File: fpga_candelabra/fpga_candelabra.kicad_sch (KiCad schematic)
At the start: 0 parts

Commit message: Candelabra: Place all FPGA symbols
Signed-off-by: Yichuan Gao <gaoyichuan000@gmail.com>
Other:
- added sheet FPGA Bank 0 (fpga_bank_0.kicad_sch)
- added sheet FPGA Bank 61-64 (fpga_bank_61_64.kicad_sch)
- added sheet FPGA Bank 65-68 (fpga_bank_65_68.kicad_sch)
- added sheet FPGA Bank 69-72 (fpga_bank_69_72.kicad_sch)
- added sheet FPGA Bank 73-74 (fpga_bank_73_74.kicad_sch)
- added sheet FPGA Power (fpga_power.kicad_sch)
- added sheet FPGA Quad 124-133 (fpga_quad_124_133.kicad_sch)
- added sheet FPGA Quad 224-233 (fpga_quad_224_233.kicad_sch)
- added sheet Power VCCINT (power_vccint.kicad_sch)

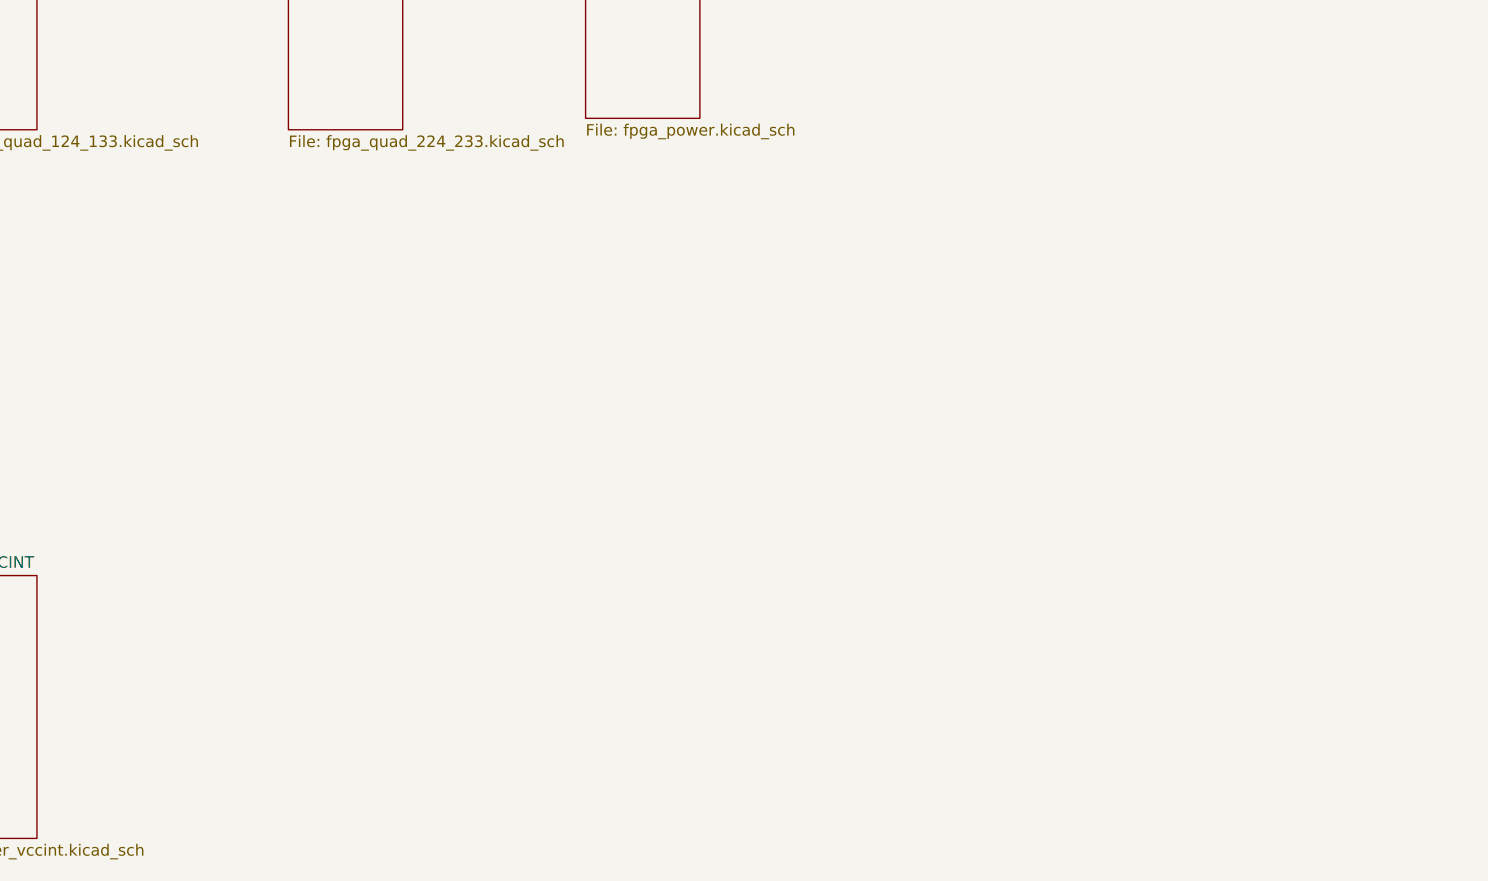
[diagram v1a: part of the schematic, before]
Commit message: fpga_candelabra: finish most FPGA & FMC VADJ power supplies
Signed-off-by: Yichuan Gao <gaoyichuan000@gmail.com>
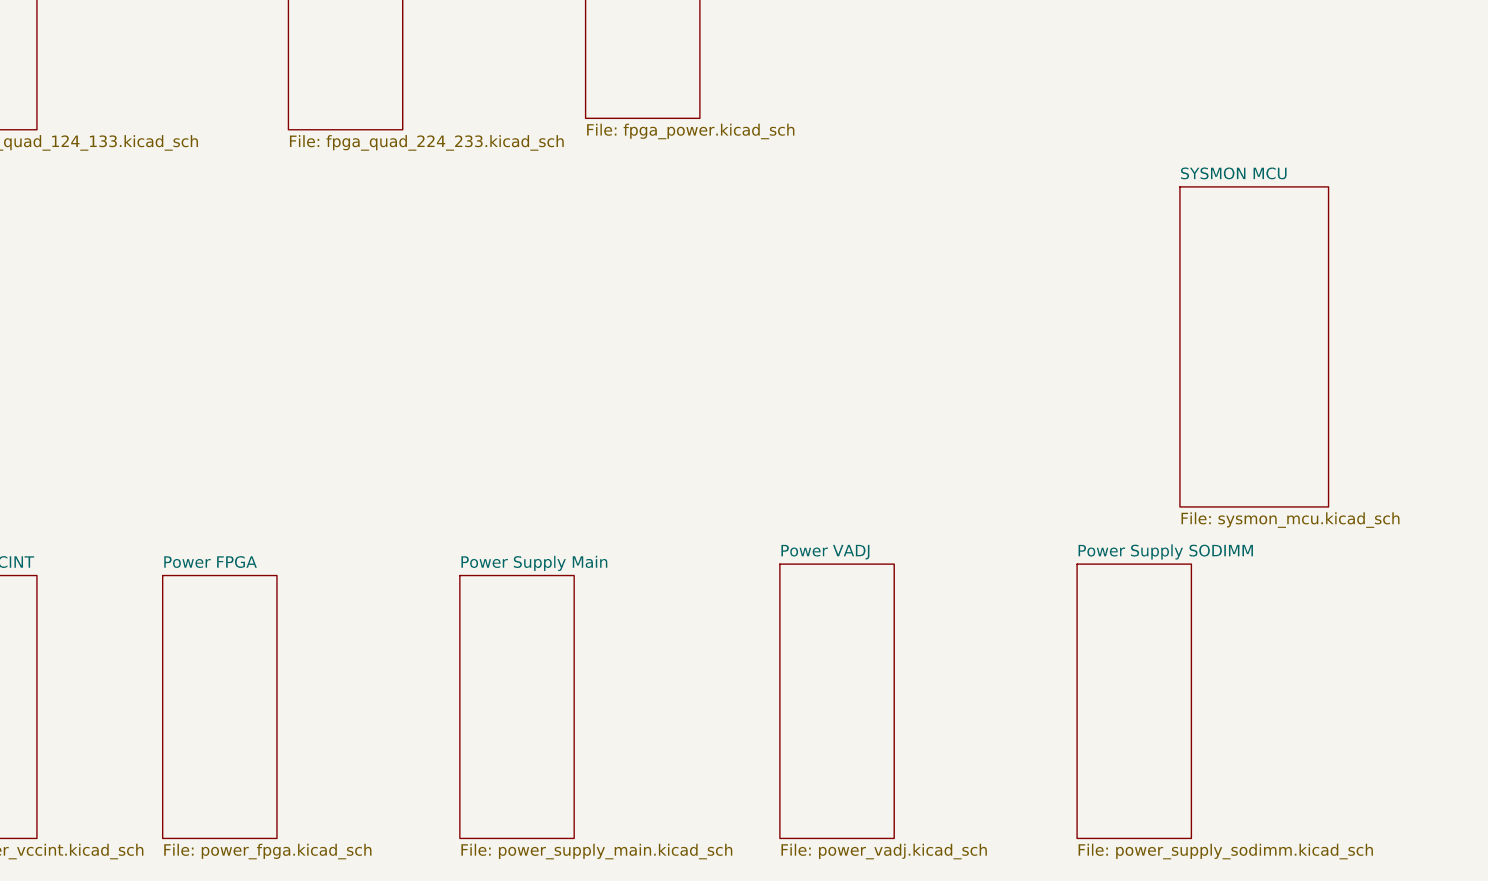
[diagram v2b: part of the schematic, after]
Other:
- added sheet Power FPGA (power_fpga.kicad_sch)
- added sheet Power Supply Main (power_supply_main.kicad_sch)
- added sheet Power Supply SODIMM (power_supply_sodimm.kicad_sch)
- added sheet Power VADJ (power_vadj.kicad_sch)
- added sheet SYSMON MCU (sysmon_mcu.kicad_sch)
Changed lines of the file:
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@@
+	)
+	(sheet
+		(at 151.13 134.62)
+		(size 12.7 30.48)
+		(fields_autoplaced yes)
+		(stroke
+			(width 0.1524)
+			(type solid)
+			(color 132 0 132 1)
+		)
+		(fill
+			(color 255 255 255 0.0000)
+		)
+		(property "Sheetname" "Power Supply SODIMM"
+			(at 151.13 133.9084 0)
+			(effects
+				(font
+					(size 1.27 1.27)
+				)
+				(justify left bottom)
+			)
+		)
+		(property "Sheetfile" "power_supply_sodimm.kicad_sch"
+			(at 151.13 165.6846 0)
+			(effects
+				(font
+					(size 1.27 1.27)
+				)
+				(justify left top)
+			)
+		)
+		(instances
+			(project "fpga_candelabra"
+				(path "/01ed9e92-4e50-4b41-90dc-10444aaec5f7"
+					(page "15")
+				)
+			)
+		)
 	)
 	(sheet
@@
 	)
 	(sheet
+		(at 82.55 135.89)
+		(size 12.7 29.21)
+		(fields_autoplaced yes)
+		(stroke
+			(width 0.1524)
+			(type solid)
+			(color 132 0 132 1)
+		)
+		(fill
+			(color 255 255 255 0.0000)
+		)
+		(property "Sheetname" "Power Supply Main"
+			(at 82.55 135.1784 0)
+			(effects
+				(font
+					(size 1.27 1.27)
+				)
+				(justify left bottom)
+			)
+		)
+		(property "Sheetfile" "power_supply_main.kicad_sch"
+			(at 82.55 165.6846 0)
+			(effects
+				(font
+					(size 1.27 1.27)
+				)
+				(justify left top)
+			)
+		)
+		(instances
+			(project "fpga_candelabra"
+				(path "/01ed9e92-4e50-4b41-90dc-10444aaec5f7"
+					(page "11")
+				)
+			)
+		)
+	)
+	(sheet
 		(at 22.86 59.69)
 		(size 12.7 26.67)
@@
 	)
 	(sheet
+		(at 162.56 92.71)
+		(size 16.51 35.56)
+		(fields_autoplaced yes)
+		(stroke
+			(width 0.1524)
+			(type solid)
+			(color 132 0 132 1)
+		)
+		(fill
+			(color 255 255 255 0.0000)
+		)
+		(property "Sheetname" "SYSMON MCU"
+			(at 162.56 91.9984 0)
+			(effects
+				(font
+					(size 1.27 1.27)
+				)
+				(justify left bottom)
+			)
+		)
+		(property "Sheetfile" "sysmon_mcu.kicad_sch"
+			(at 162.56 128.8546 0)
+			(effects
+				(font
+					(size 1.27 1.27)
+				)
+				(justify left top)
+			)
+		)
+		(instances
+			(project "fpga_candelabra"
+				(path "/01ed9e92-4e50-4b41-90dc-10444aaec5f7"
+					(page "10")
+				)
+			)
+		)
+	)
+	(sheet
 		(at 50.8 20.32)
 		(size 12.7 25.4)
@@
 	)
 	(sheet
+		(at 49.53 135.89)
+		(size 12.7 29.21)
+		(fields_autoplaced yes)
+		(stroke
+			(width 0.1524)
+			(type solid)
+			(color 132 0 132 1)
+		)
+		(fill
+			(color 255 255 255 0.0000)
+		)
+		(property "Sheetname" "Power FPGA"
+			(at 49.53 135.1784 0)
+			(effects
+				(font
+					(size 1.27 1.27)
+				)
+				(justify left bottom)
+			)
+		)
+		(property "Sheetfile" "power_fpga.kicad_sch"
+			(at 49.53 165.6846 0)
+			(effects
+				(font
+					(size 1.27 1.27)
+				)
+				(justify left top)
+			)
+		)
+		(instances
+			(project "fpga_candelabra"
+				(path "/01ed9e92-4e50-4b41-90dc-10444aaec5f7"
+					(page "13")
+				)
+			)
+		)
+	)
+	(sheet
 		(at 96.52 59.69)
 		(size 12.7 25.4)
@@
 			(project "fpga_candelabra"
 				(path "/01ed9e92-4e50-4b41-90dc-10444aaec5f7"
-					(page "10")
-				)
-			)
+					(page "12")
+				)
+			)
+		)
+	)
+	(sheet
+		(at 118.11 134.62)
+		(size 12.7 30.48)
+		(fields_autoplaced yes)
+		(stroke
+			(width 0.1524)
+			(type solid)
+			(color 132 0 132 1)
+		)
+		(fill
+			(color 255 255 255 0.0000)
+		)
+		(property "Sheetname" "Power VADJ"
+			(at 118.11 133.9084 0)
+			(effects
+				(font
+					(size 1.27 1.27)
+				)
+				(justify left bottom)
+			)
+		)
+		(property "Sheetfile" "power_vadj.kicad_sch"
+			(at 118.11 165.6846 0)
+			(effects
+				(font
+					(size 1.27 1.27)
+				)
+				(justify left top)
+			)
+		)
+		(instances
+			(project "fpga_candelabra"
+				(path "/01ed9e92-4e50-4b41-90dc-10444aaec5f7"
+					(page "14")
+				)
+			)

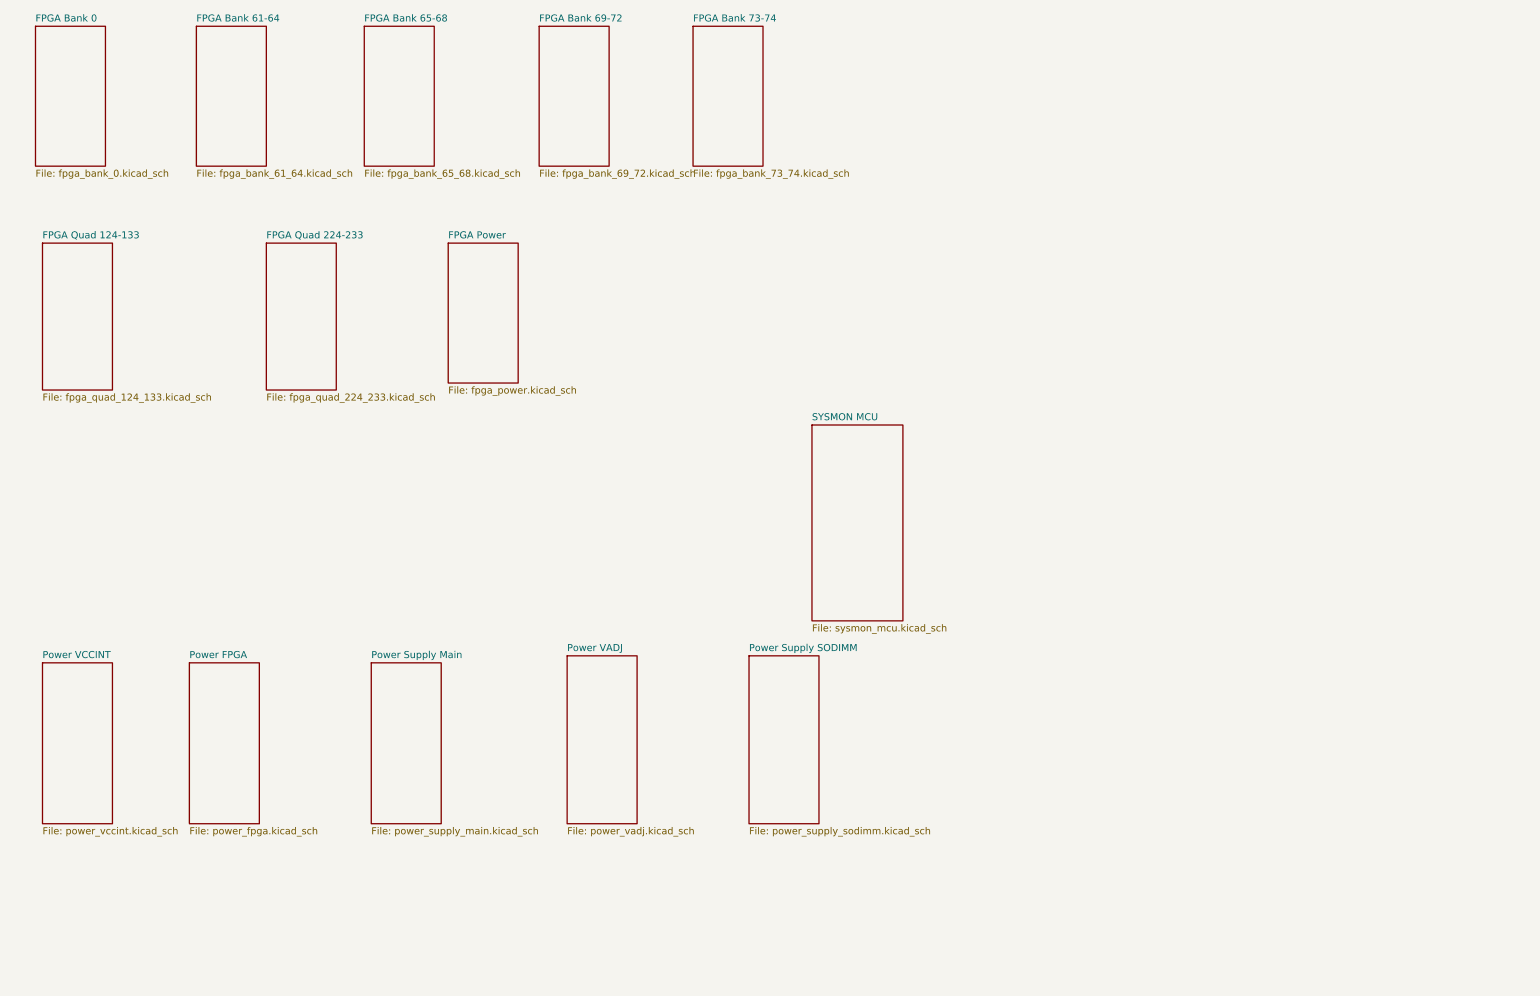
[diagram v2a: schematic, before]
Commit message: fpga_candelabra: add ddr4 power and sysmon mcu periph, bump library
Signed-off-by: Yichuan Gao <gaoyichuan000@gmail.com>
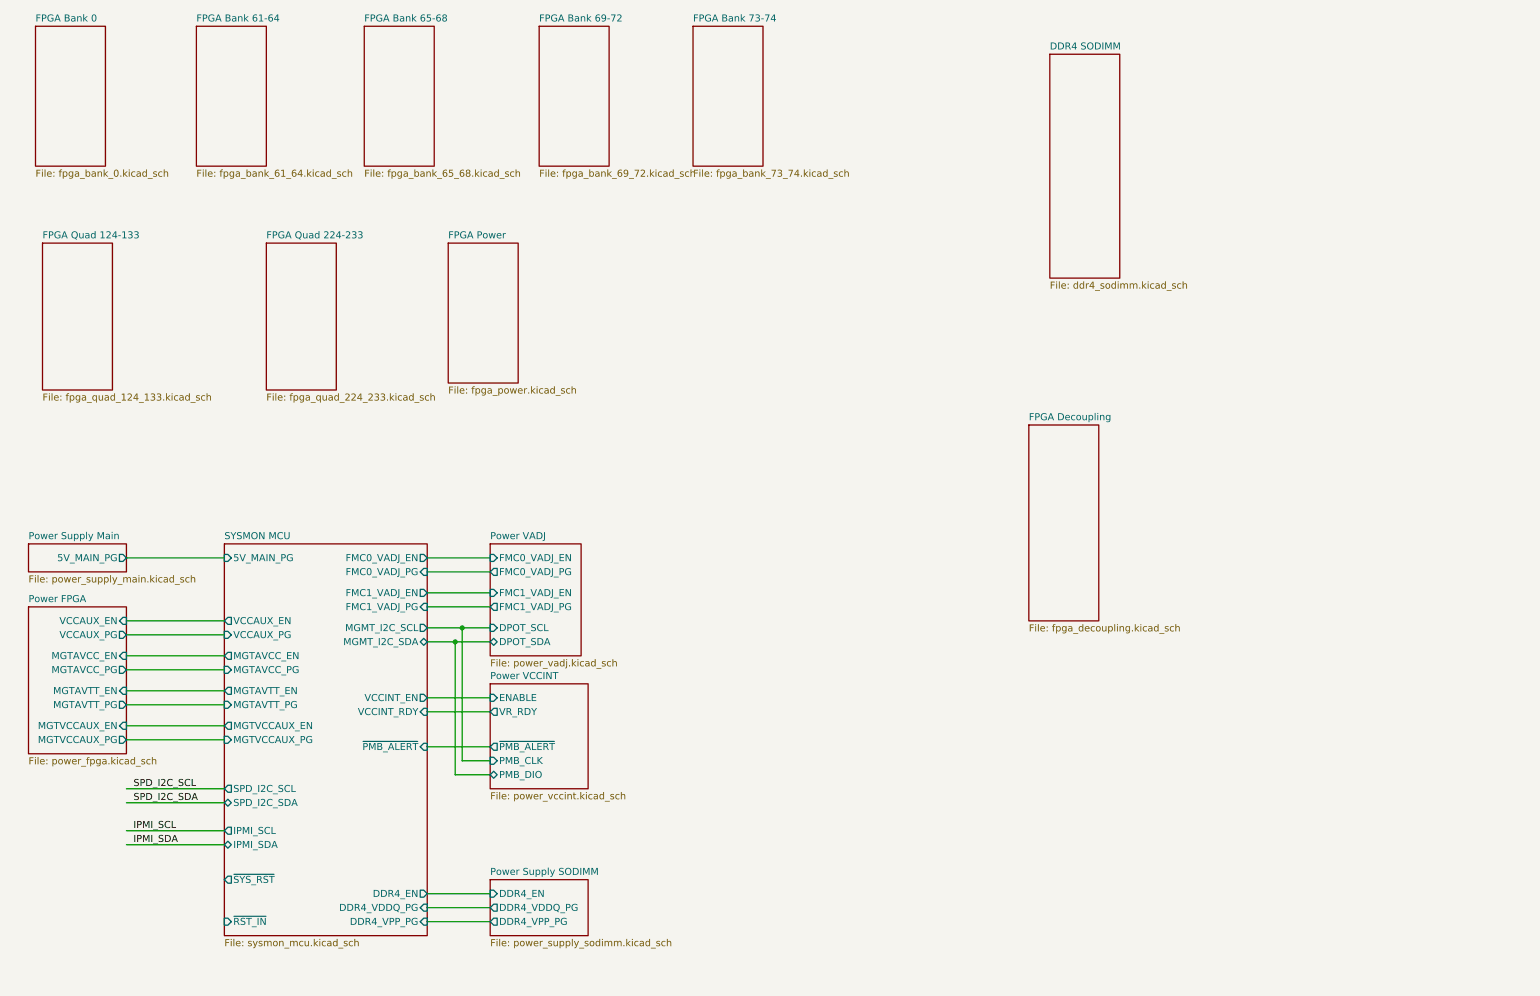
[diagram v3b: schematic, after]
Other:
- added sheet DDR4 SODIMM (ddr4_sodimm.kicad_sch)
- added sheet FPGA Decoupling (fpga_decoupling.kicad_sch)
- sheet Power FPGA ports: added MGTAVCC_EN, MGTAVCC_PG, MGTAVTT_EN, MGTAVTT_PG, MGTVCCAUX_EN, MGTVCCAUX_PG, VCCAUX_EN, VCCAUX_PG; removed none
- sheet Power Supply Main ports: added 5V_MAIN_PG; removed none
- sheet Power Supply SODIMM ports: added DDR4_EN, DDR4_VDDQ_PG, DDR4_VPP_PG; removed none
- sheet Power VADJ ports: added DPOT_SCL, DPOT_SDA, FMC0_VADJ_EN, FMC0_VADJ_PG, FMC1_VADJ_EN, FMC1_VADJ_PG; removed none
- sheet Power VCCINT ports: added ENABLE, PMB_CLK, PMB_DIO, VR_RDY, ~{PMB_ALERT}; removed none
- sheet SYSMON MCU ports: added 5V_MAIN_PG, DDR4_EN, DDR4_VDDQ_PG, DDR4_VPP_PG, FMC0_VADJ_EN, FMC0_VADJ_PG, FMC1_VADJ_EN, FMC1_VADJ_PG, IPMI_SCL, IPMI_SDA, MGMT_I2C_SCL, MGMT_I2C_SDA, MGTAVCC_EN, MGTAVCC_PG, MGTAVTT_EN, MGTAVTT_PG, MGTVCCAUX_EN, MGTVCCAUX_PG, SPD_I2C_SCL, SPD_I2C_SDA, VCCAUX_EN, VCCAUX_PG, VCCINT_EN, VCCINT_RDY, ~{PMB_ALERT}, ~{RST_IN}, ~{SYS_RST}; removed none
